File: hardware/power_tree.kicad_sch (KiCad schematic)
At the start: 0 parts

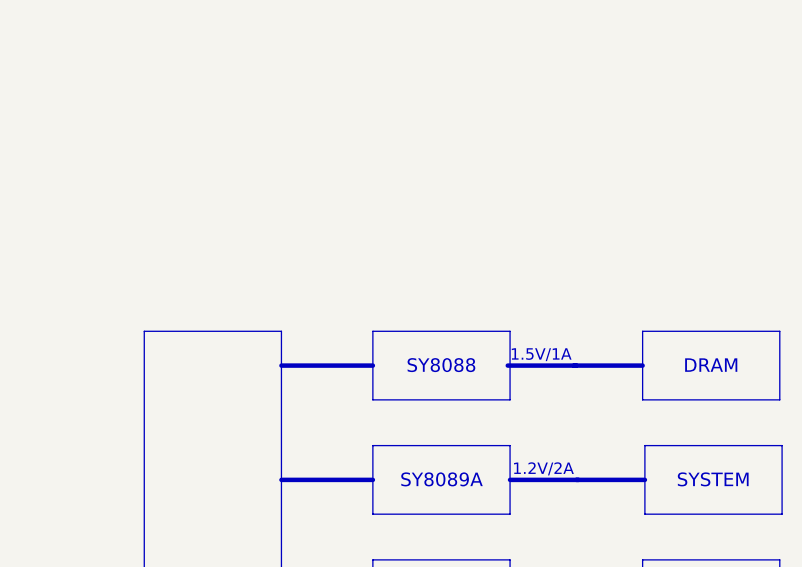
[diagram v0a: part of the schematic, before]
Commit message: Update crystal
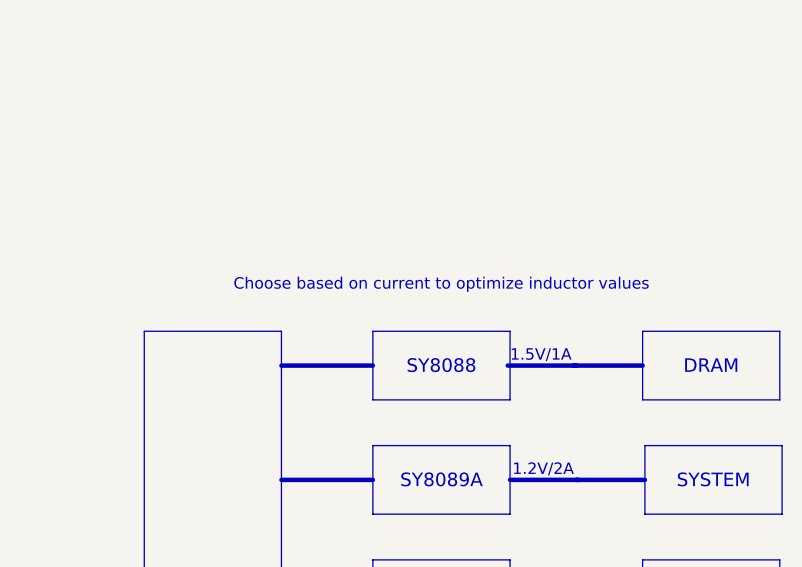
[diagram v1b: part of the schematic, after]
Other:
- note added: "Choose based on current to optimize inductor values"
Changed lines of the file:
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@@
 		(comment 3 "License: Solderpad")
+	)
+	(text "Choose based on current to optimize inductor values"
+		(exclude_from_sim no)
+		(at 134.62 45.72 0)
+		(effects
+			(font
+				(size 1.27 1.27)
+			)
+		)
 	)
 	(text "1.2V/2A"

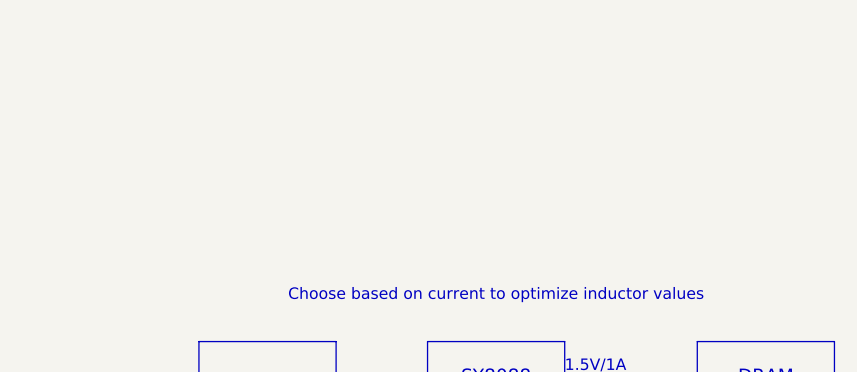
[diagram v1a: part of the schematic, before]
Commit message: Add schematic pdf
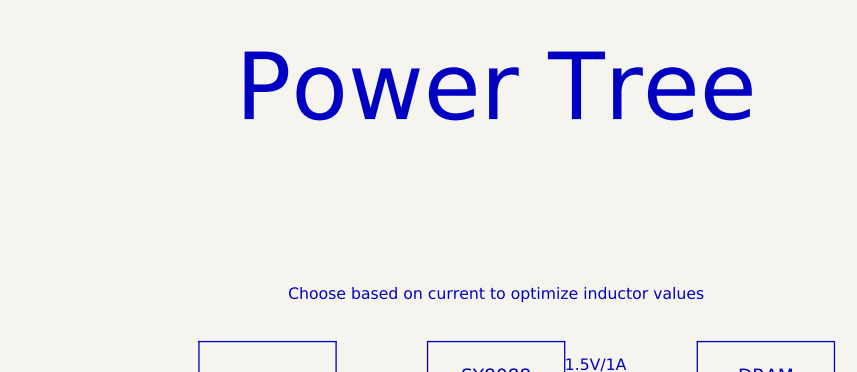
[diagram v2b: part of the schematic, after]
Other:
- note added: "Power Tree"
- title: Icepi CM0 -> Icepi SBC
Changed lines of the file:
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@@
 	(paper "A4")
 	(title_block
-		(title "Icepi CM0")
-		(date "2025-11-21")
+		(title "Icepi SBC")
+		(date "2025-12-21")
 		(rev "v1.0")
 		(company "Icy Electronics")
 		(comment 1 "Chengyin Yao (cheyao)")
-		(comment 2 "https://github.com/cheyao/icepi-cm0")
+		(comment 2 "https://github.com/cheyao/icepi-sbc")
 		(comment 3 "License: Solderpad")
 	)
@@
 		)
 	)
+	(text "Power Tree"
+		(exclude_from_sim no)
+		(at 134.62 22.86 0)
+		(effects
+			(font
+				(face "Fira Sans Medium")
+				(size 7.5 7.5)
+			)
+		)
+	)
